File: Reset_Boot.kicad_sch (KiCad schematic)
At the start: 24 parts, among them J301 Micro_SD_Card, J302 Molex PicoBlade 4-pin, Q301 BSS138PW,115, SW301 KMR2, SW302 KMR2, U301 SSM2518CPZ

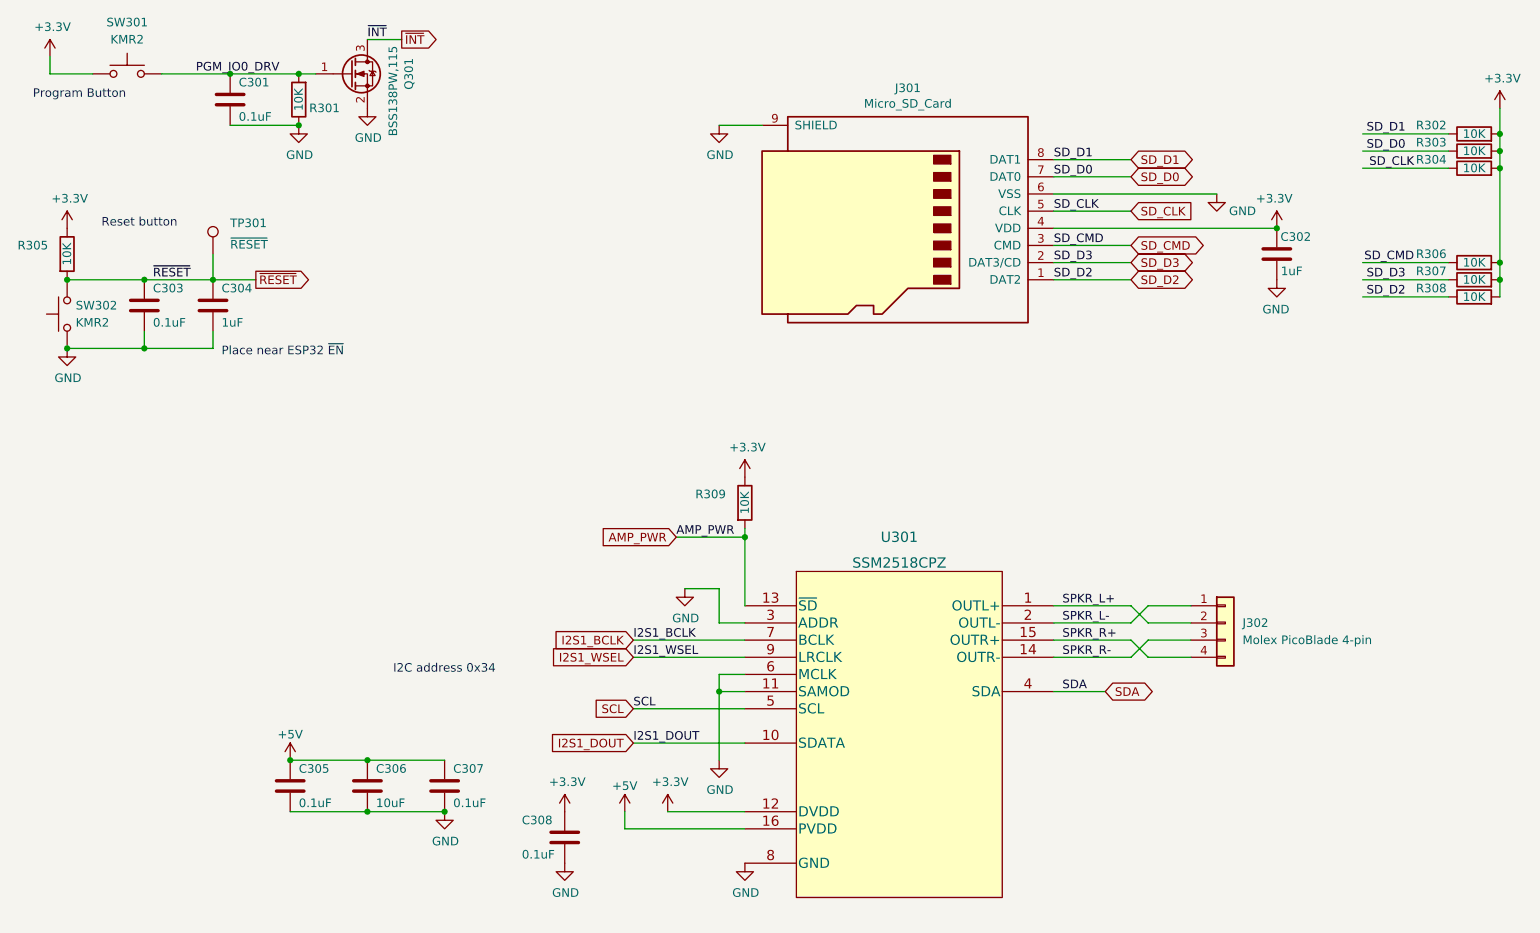
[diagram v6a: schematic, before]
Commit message: Moved to ESP32 S3 Wroom 1
The Wroom 2 requires 1.8V on a couple of GPIOs.  Since I don't need 32MB of
flash the Wroom 1 is used instead.  The footprint is slightly different,
however.

Signed-off-by: Aaron Williams <aaron.w2@gmail.com>
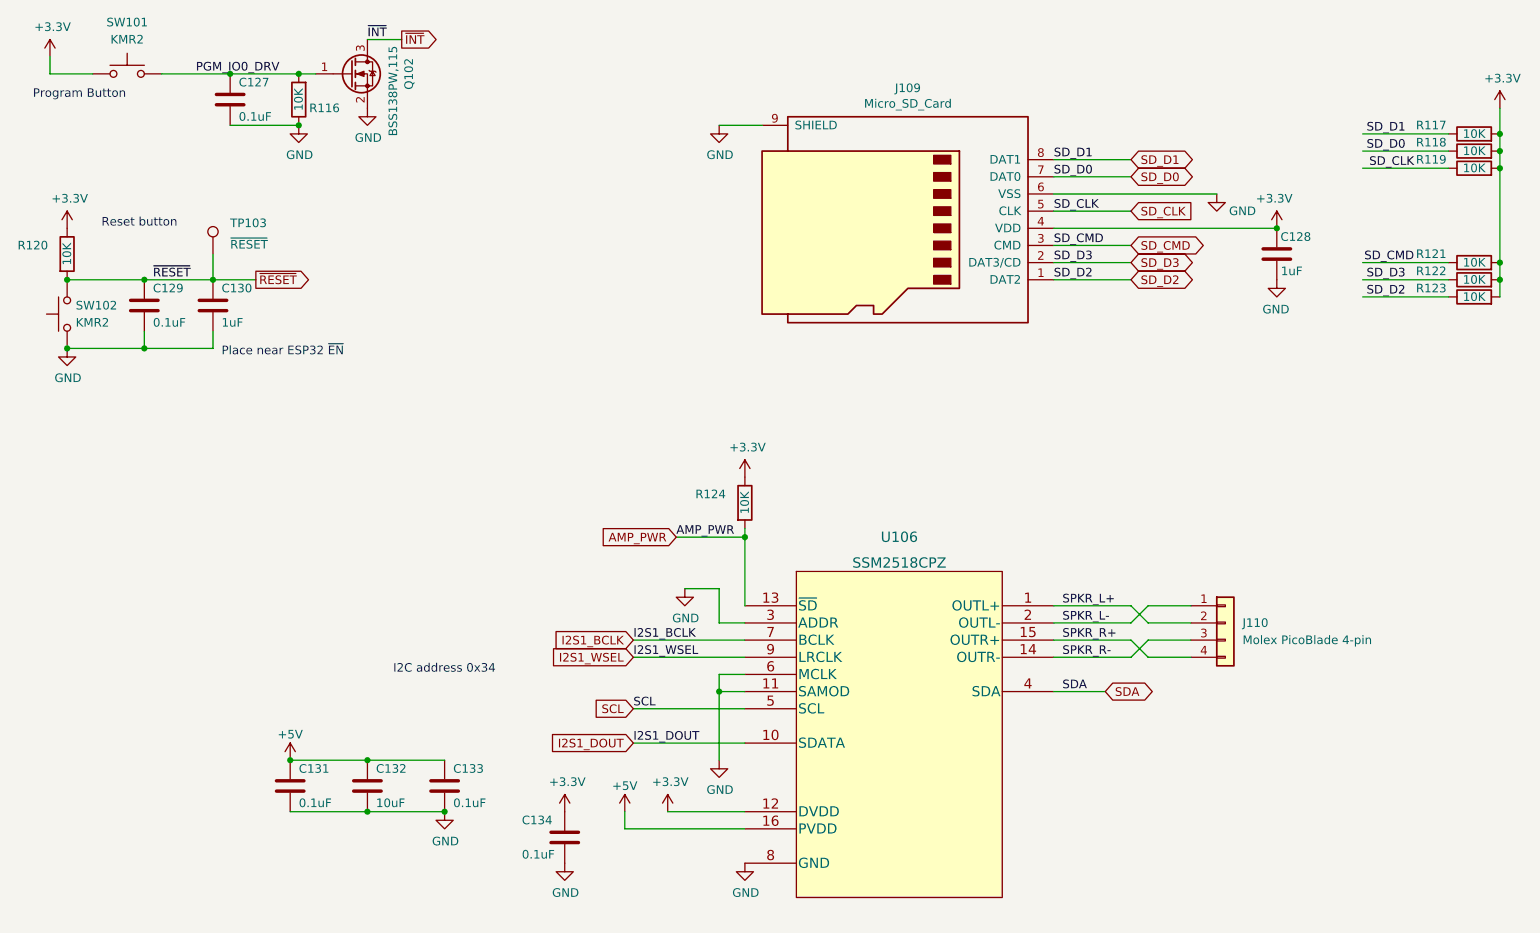
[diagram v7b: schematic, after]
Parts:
- renumbered C301 to C127, C302 to C128, C303 to C129, C304 to C130, C305 to C131, C306 to C132, C307 to C133, C308 to C134, J301 to J109, J302 to J110, Q301 to Q102, R301 to R116, R302 to R117, R303 to R118, R304 to R119, R305 to R120, R306 to R121, R307 to R122, R308 to R123, R309 to R124, SW301 to SW101, SW302 to SW102, TP301 to TP103, U301 to U106
